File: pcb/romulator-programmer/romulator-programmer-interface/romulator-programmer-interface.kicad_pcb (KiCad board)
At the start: 2 copper layers, 35.8 x 26.9 mm, 4 parts, among them J1 Conn_01x02_Male, J2 Conn_01x01_Male, J3 Conn_02x05_Odd_Even, U1 WeMos_D1_mini

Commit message: new adapters
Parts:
- J2: value Conn_01x01_Male -> Conn_01x02_Male; footprint Connector_PinHeader_2.54mm:PinHeader_1x01_P2.54mm_Vertical -> Connector_PinHeader_2.54mm:PinHeader_1x02_P2.54mm_Vertical
- J3: value Conn_02x05_Odd_Even -> Conn_02x08_Odd_Even; footprint Connector_PinHeader_2.54mm:PinHeader_2x05_P2.54mm_Vertical -> Connector_PinHeader_2.54mm:PinHeader_2x08_P2.54mm_Vertical
- moved J2 7.91 mm to (165.7, 96.8), turned to 270 degrees
- moved J3 4.89 mm to (165.7, 89.2)
- moved J1 1.37 mm to (165.7, 93.0), turned to 270 degrees
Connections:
- J3 pad 6: Net-(J3-Pad6) -> CDONE
- U1 pad 13: Net-(U1-Pad13) -> CDONE
- U1 pad 9: +5V -> 5VIN
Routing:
- net 5VIN: track 0.00 -> 31.2 mm
- net CDONE: track 0.00 -> 25.2 mm
- net RST: track 34.1 -> 25.4 mm
- net +5V: track 35.1 -> 26.6 mm
- net +3V3: track 10.8 -> 5.50 mm
- net CS: track 32.8 -> 37.7 mm
- net 3v3IN: track 41.3 -> 38.0 mm
- net MISO: track 25.7 -> 28.4 mm
- net SCK: track 23.1 -> 25.8 mm
- net DBG: track 19.9 -> 22.7 mm
- net MOSI: track 31.3 -> 34.1 mm
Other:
- board size 35.8 x 26.9 mm -> 37.6 x 29.3 mm
- board text added: "3v3"
- board text added: "5V"
- board text added: "5v"
- board text added: "CDONE"
- board text added: "CS"
- board text added: "DBG"
- board text added: "GND"
- board text added: "MISO"
- board text added: "MOSI"
- board text added: "ROMulator Program/Debug"
- board text added: "RST"
- board text added: "SCK"

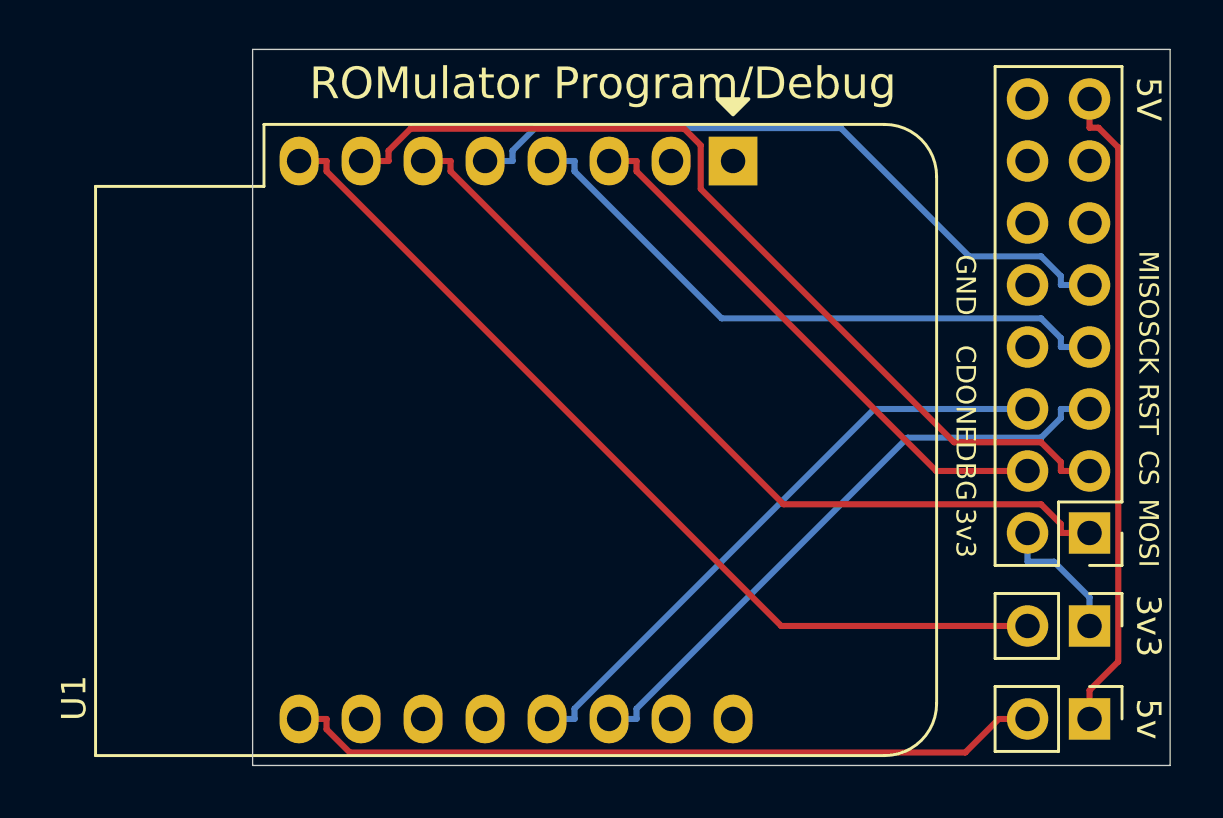
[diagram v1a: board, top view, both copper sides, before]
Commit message: fixed programmer board layout
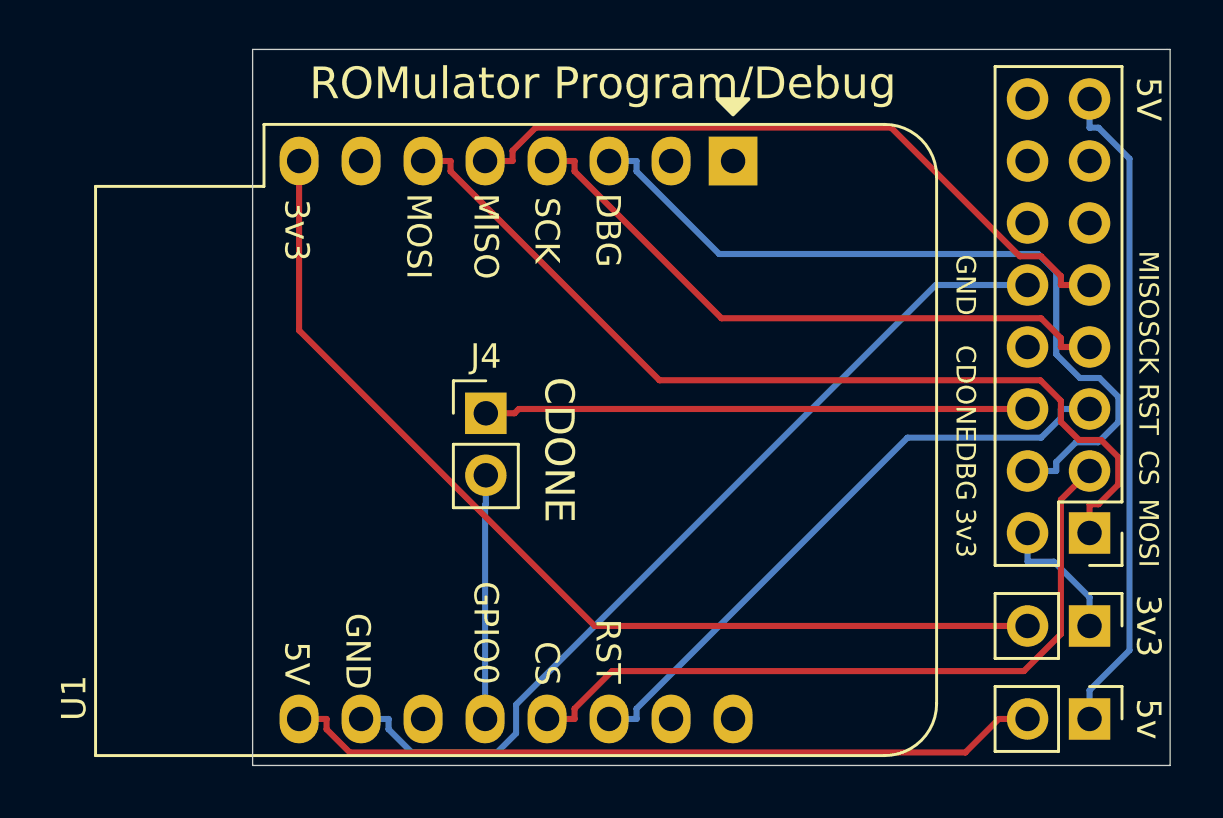
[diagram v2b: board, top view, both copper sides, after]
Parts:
- added J4: Conn_01x02_Male, Connector_PinHeader_2.54mm:PinHeader_1x02_P2.54mm_Vertical, F.Cu at (141.0, 84.2)
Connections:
- net Net-(U1-Pad11) renamed LED
- U1 pad 10: Net-(U1-Pad10) -> GND
- U1 pad 12: Net-(U1-Pad12) -> GPIO0
- U1 pad 13: CDONE -> CS
- U1 pad 7: CS -> Net-(U1-Pad7)
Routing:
- net GND: track 0.00 -> 36.7 mm
- net DBG: track 22.7 -> 32.9 mm
- net GPIO0: track 0.00 -> 10.00 mm
- net CS: track 37.7 -> 29.9 mm
- net MOSI: track 34.1 -> 38.1 mm
- net 3v3IN: track 38.0 -> 41.8 mm
- net CDONE: track 25.2 -> 22.3 mm
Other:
- board text added: "GPIO0"

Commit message: added silkscreen on programmer pcb
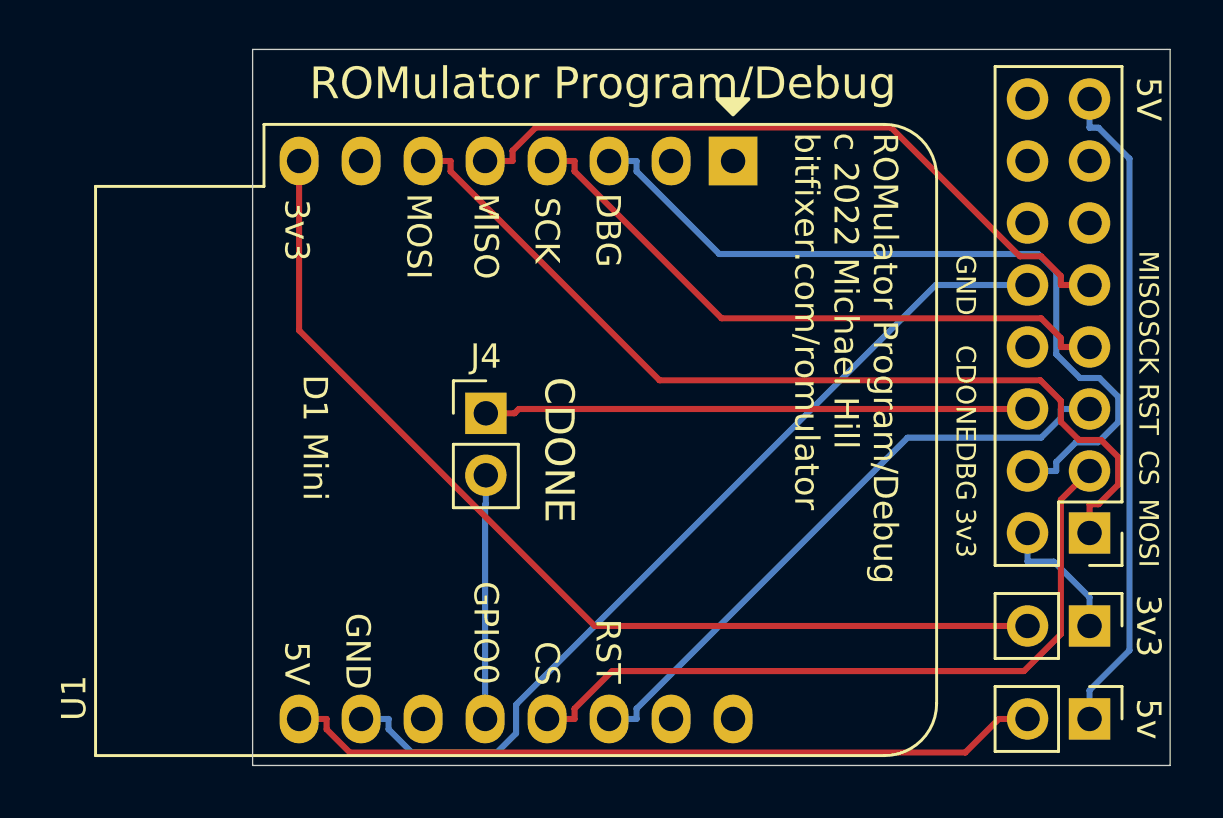
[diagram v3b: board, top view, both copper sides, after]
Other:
- board text added: "D1 Mini"
- board text added: "ROMulator Program/Debug c 2022 Michael Hill bitfixer.com/romulator"
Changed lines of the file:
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@@
   (general
     (thickness 1.6)
-    (drawings 29)
+    (drawings 31)
     (tracks 91)
     (zones 0)
@@
     )
   )
+  (gr_text "D1 Mini" (at 134 85.25 270) (layer F.SilkS)
+    (effects (font (size 1 1) (thickness 0.15)))
+  )
+  (gr_text "ROMulator Program/Debug\nc 2022 Michael Hill\nbitfixer.com/romulator" (at 155.75 72.75 270) (layer F.SilkS)
+    (effects (font (size 1 1) (thickness 0.15)) (justify left))
+  )
   (gr_text GND (at 135.75 94 270) (layer F.SilkS)
